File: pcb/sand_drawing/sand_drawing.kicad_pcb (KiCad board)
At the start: 2 copper layers, 54.2 x 81.5 mm, 41 parts, among them J0 12V GND, J1 Stepper1, J2 Stepper2, J3 Opto 1, J4 Opto 2, J5 UART, SW1 EN, SW2 IO0, U1 AP63203WU, U2 ESP32-WROOM-32D

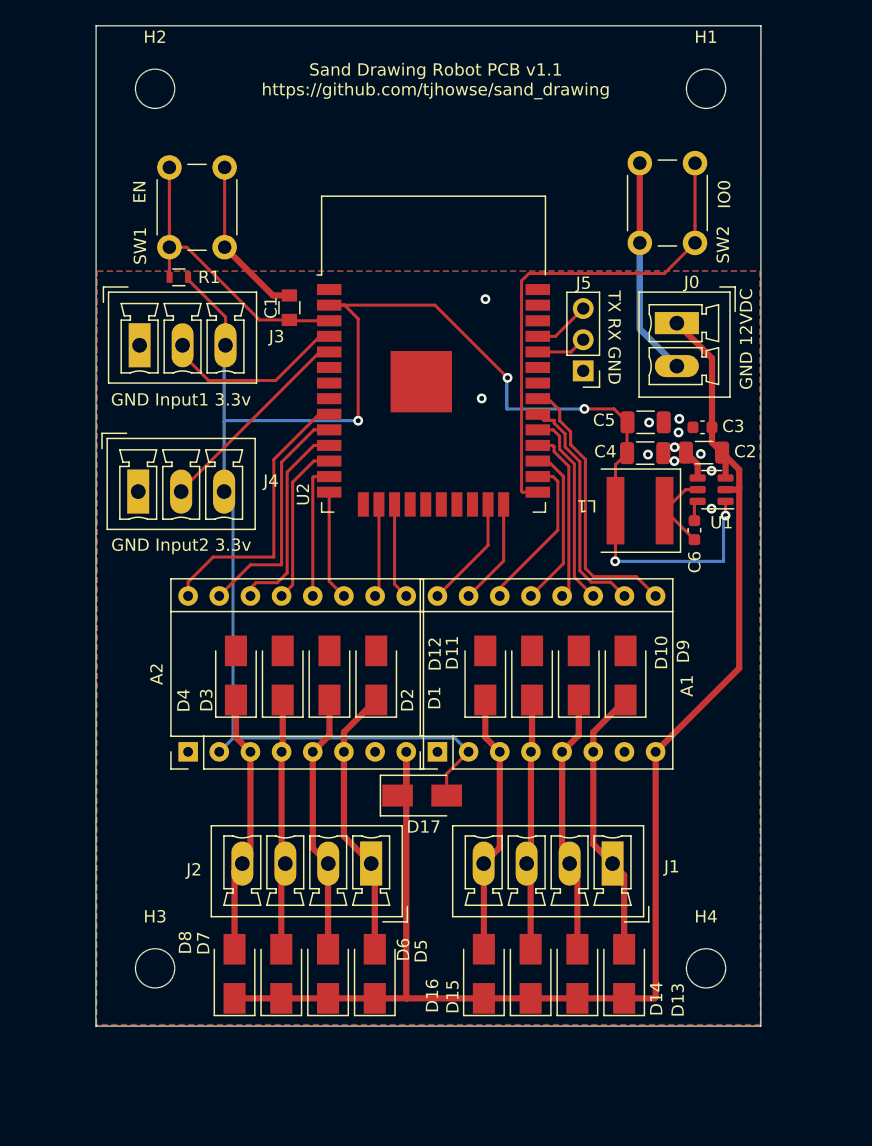
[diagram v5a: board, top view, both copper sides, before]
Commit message: Updated to kicad v7.0.8.
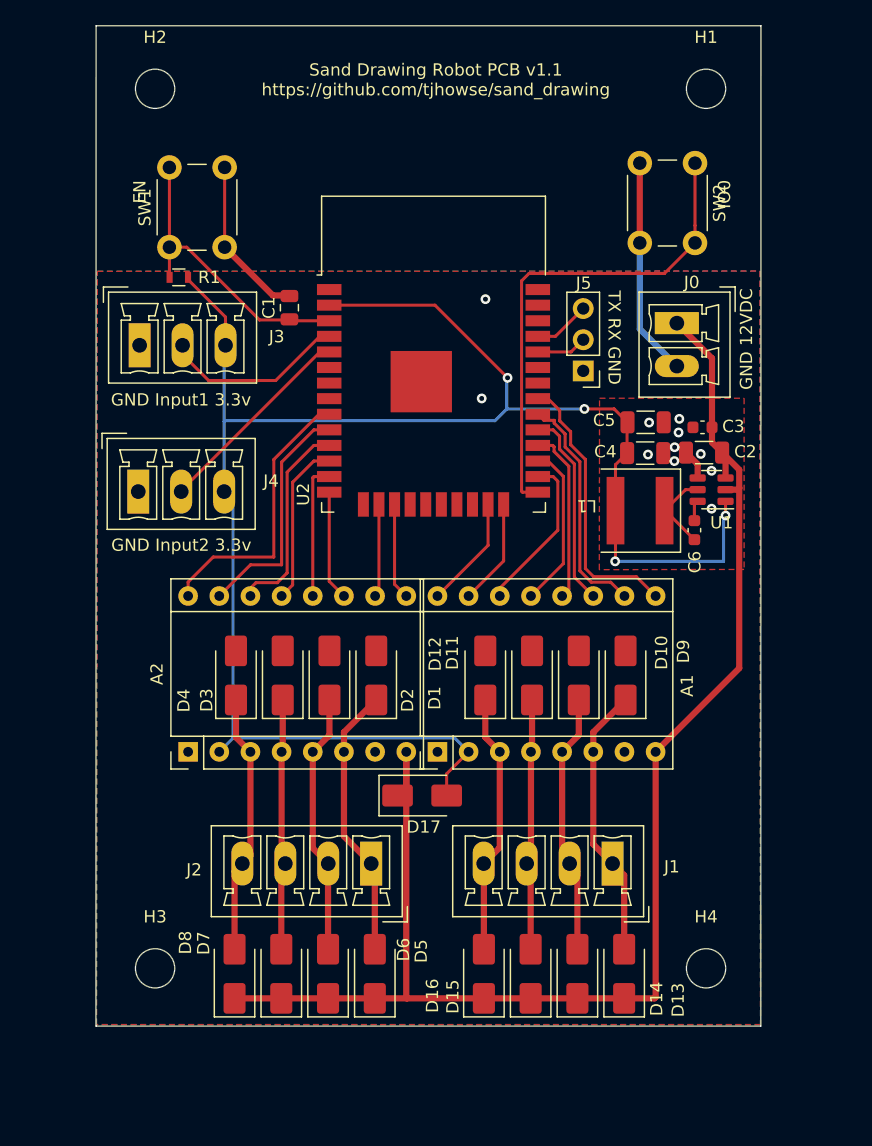
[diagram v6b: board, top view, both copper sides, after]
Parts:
- C1: footprint Capacitors_SMD:C_0805 -> Capacitor_SMD:C_0805_2012Metric
- SW1, SW2: footprint Buttons_Switches_THT:SW_PUSH_6mm -> Button_Switch_THT:SW_PUSH_6mm
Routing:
- net +3V3: track 142.0 -> 143.4 mm, vias 5 -> 4

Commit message: Update footprints.
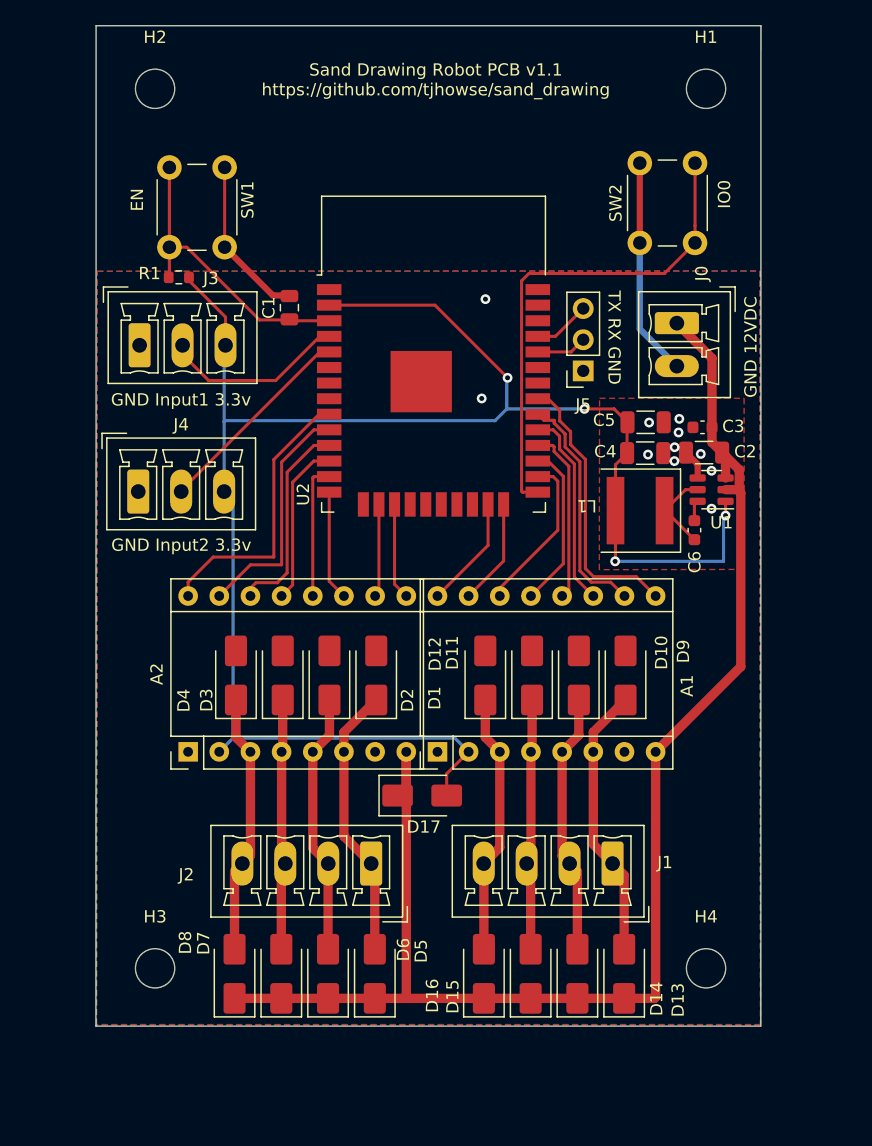
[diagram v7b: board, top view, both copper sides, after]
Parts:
- H1, H2, H3, H4: footprint Mounting_Holes:MountingHole_3.2mm_M3 -> MountingHole:MountingHole_3.2mm_M3
- J0: footprint Connectors_Phoenix:PhoenixContact_MCV-G_02x3.50mm_Vertical -> Connector_Phoenix_MC:PhoenixContact_MCV_1,5_2-G-3.5_1x02_P3.50mm_Vertical
- J1, J2: footprint Connectors_Phoenix:PhoenixContact_MCV-G_04x3.50mm_Vertical -> Connector_Phoenix_MC:PhoenixContact_MCV_1,5_4-G-3.5_1x04_P3.50mm_Vertical
- J3, J4: footprint Connectors_Phoenix:PhoenixContact_MCV-G_03x3.50mm_Vertical -> Connector_Phoenix_MC:PhoenixContact_MCV_1,5_3-G-3.5_1x03_P3.50mm_Vertical
- J5: footprint Socket_Strips:Socket_Strip_Straight_1x03_Pitch2.54mm -> Connector_PinSocket_2.54mm:PinSocket_1x03_P2.54mm_Vertical
- R1: footprint Resistors_SMD:R_0603 -> Resistor_SMD:R_0603_1608Metric

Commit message: Tweaks
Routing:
- net GND: track 33.7 -> 25.8 mm
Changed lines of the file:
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@@
   (via (at 145.92 109.71) (size 0.8) (drill 0.4) (layers "F.Cu" "B.Cu") (free) (net 1))
   (via (at 144.11 107.96) (size 0.8) (drill 0.4) (layers "F.Cu" "B.Cu") (free) (net 1))
-  (segment (start 140.95 92.51) (end 140.95 99.53) (width 0.508) (layer "B.Cu") (net 1))
-  (segment (start 140.95 99.53) (end 143.97 102.55) (width 0.508) (layer "B.Cu") (net 1))
+  (segment (start 140.95 92.51) (end 140.95 95.95) (width 0.508) (layer "B.Cu") (net 1))
   (segment (start 107.188 101.6) (end 107.188 98.552) (width 0.25) (layer "F.Cu") (net 2))
   (segment (start 107.188 98.552) (end 104.14 95.504) (width 0.25) (layer "F.Cu") (net 2))
